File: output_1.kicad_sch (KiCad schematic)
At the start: 5 parts, among them U302 MIC2097-1YMT-TR

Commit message: Update CC resistors with feedback
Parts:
- TP? (x2): footprint 2usb:TestPoint_SM -> 2usb:TestPoint_MD
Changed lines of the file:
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@@
       (effects (font (size 1.27 1.27)) (justify right))
     )
-    (property "Footprint" "2usb:TestPoint_SM" (at 106.68 104.14 0)
+    (property "Footprint" "2usb:TestPoint_MD" (at 106.68 104.14 0)
       (effects (font (size 1.27 1.27)) hide)
     )
@@
       (effects (font (size 1.27 1.27)) (justify left))
     )
-    (property "Footprint" "2usb:TestPoint_SM" (at 116.84 101.6 0)
+    (property "Footprint" "2usb:TestPoint_MD" (at 116.84 101.6 0)
       (effects (font (size 1.27 1.27)) hide)
     )

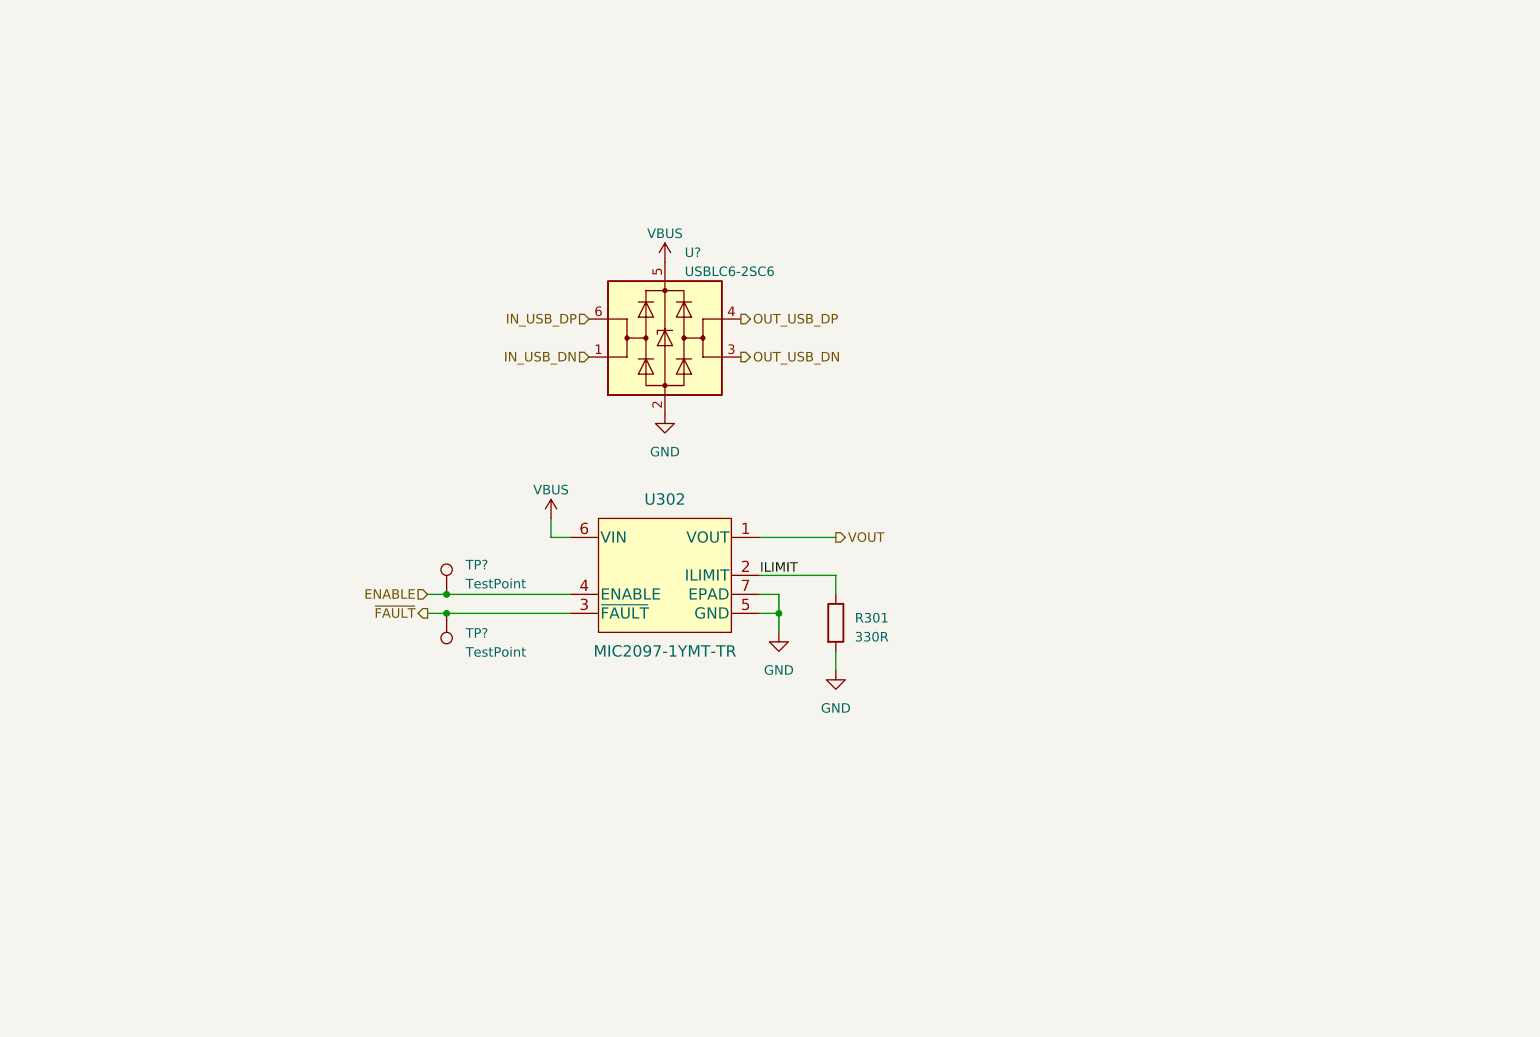
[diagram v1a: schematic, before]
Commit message: Add power switch ic and channel config ic
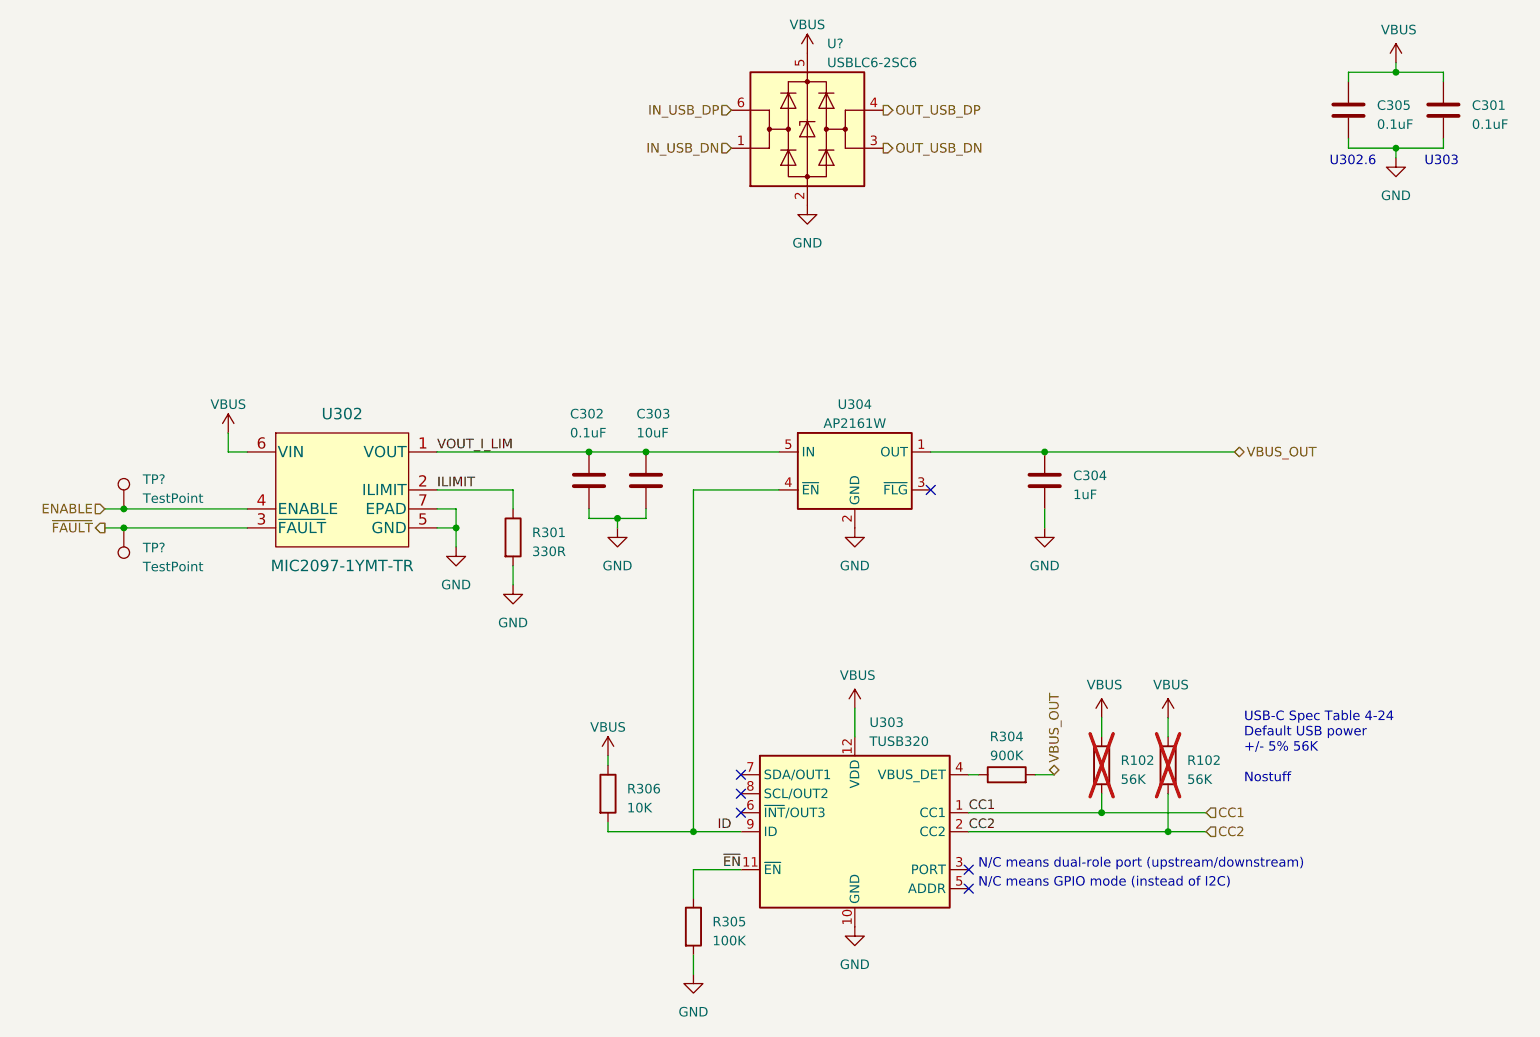
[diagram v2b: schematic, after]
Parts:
- added C301, C302, C305: 0.1uF, Capacitor_SMD:C_0201_0603Metric, symbol Device:C
- added C303: 10uF, Capacitor_SMD:C_0201_0603Metric, symbol Device:C
- added C304: 1uF, Capacitor_SMD:C_0201_0603Metric, symbol Device:C
- added R102 (x2): 56K, Resistor_SMD:R_0201_0603Metric, symbol Device:R
- added R304: 900K, Resistor_SMD:R_0201_0603Metric, symbol Device:R
- added R305: 100K, Resistor_SMD:R_0201_0603Metric, symbol Device:R
- added R306: 10K, symbol Device:R
- added U303: TUSB320, Package_DFN_QFN:Texas_X2QFN-12_1.6x1.6mm_P0.4mm, symbol Interface_USB:TUSB320
- added U304: AP2161W, symbol Power_Management:AP2161W
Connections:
- net GND: now also C301.1, C302.1, C303.1, C304.1, C305.1, R305.2, U303.10 (GND), U304.2 (GND)
- net VBUS: now also C301.2, C305.2, R102.2, R102.2, R306.1, U303.12 (VDD)
- net VOUT renamed VOUT_I_LIM
- net VOUT_I_LIM: now also C302.2, C303.2, U304.5 (IN)
- new net: R304.1, U303.4 (VBUS_DET)
- new net CC1: R102.1, U303.1 (CC1)
- new net CC2: R102.1, U303.2 (CC2)
- new net ID: R306.2, U303.9 (ID), U304.4 (~{EN})
- new net VBUS_OUT: C304.2, R304.2, U304.1 (OUT)
- new net ~{EN}: R305.1, U303.11 (~{EN})
- no-connect marks 0 -> 6
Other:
- note added: "N/C means GPIO mode (instead of I2C)"
- note added: "N/C means dual-role port (upstream/downstream)"
- note added: "U302.6"
- note added: "U303"
- note added: "USB-C Spec Table 4-24 Default USB power +/- 5% 56K Nostuff"
- moved on the sheet: R301, TP?, U302, U?

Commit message: Layout checkpoint
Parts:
- removed U304: AP2161W, symbol Power_Management:AP2161W
- added U304: AP2161W, 2usb:SON50P181X201X60-7N, symbol 2usb:AP2161W
- R306: footprint (none) -> Resistor_SMD:R_0201_0603Metric
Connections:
- net GND: now also U304.1 (GND), U304.7 (PAD)
- net ID: now also U304.3 (~{FLG})
- net VBUS_OUT: now also U304.5 (OUT), U304.6 (OUT)
- net VOUT_I_LIM: now also U304.2 (IN)
- net VBUS_DET: now reaches R304.1, U303.4 (VBUS_DET)
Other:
- moved on the sheet: R102, R304

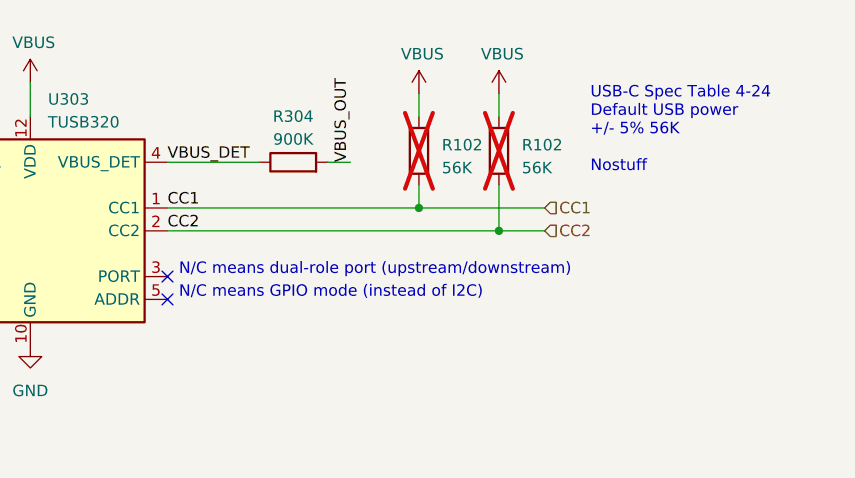
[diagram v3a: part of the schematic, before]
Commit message: Update schematic with feedback
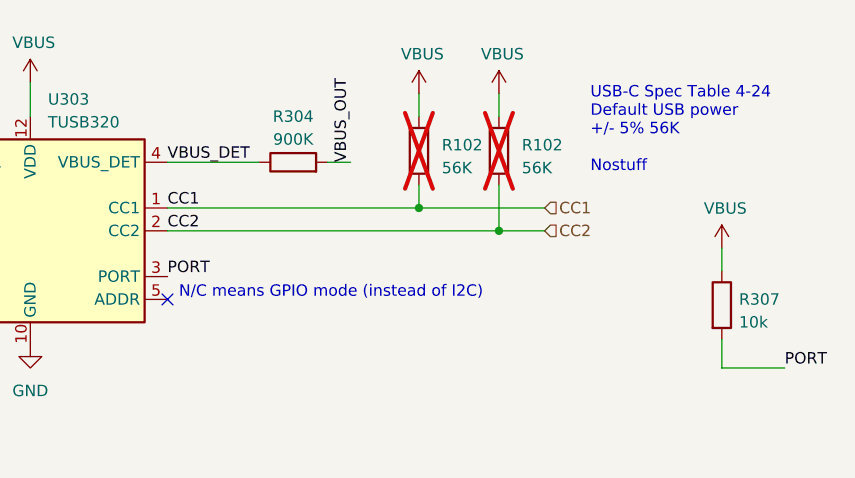
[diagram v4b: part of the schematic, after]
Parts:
- added R307: 10k, Resistor_SMD:R_0201_0603Metric, symbol Device:R
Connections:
- net VBUS: now also R307.1
- net PORT: now reaches U303.3 (PORT)
- net PORT: now also R307.2
- no-connect marks 6 -> 5
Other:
- note removed: "N/C means dual-role port (upstream/downstream)"
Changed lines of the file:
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@@
   )
   (no_connect (at 151.13 128.27))
-  (no_connect (at 181.61 138.43))
   (no_connect (at 151.13 130.81))
   (no_connect (at 151.13 125.73))
@@
     (stroke (width 0) (type default))
   )
+  (wire (pts (xy 243.205 135.255) (xy 243.205 137.795))
+    (stroke (width 0) (type default))
+  )
   (wire (pts (xy 133.35 132.08) (xy 133.35 133.35))
     (stroke (width 0) (type default))
@@
     (stroke (width 0) (type default))
   )
+  (wire (pts (xy 243.205 148.59) (xy 250.19 148.59))
+    (stroke (width 0) (type default))
+  )
   (wire (pts (xy 133.35 133.35) (xy 144.78 133.35))
     (stroke (width 0) (type default))
@@
   )
   (wire (pts (xy 134.62 91.44) (xy 134.62 92.71))
+    (stroke (width 0) (type default))
+  )
+  (wire (pts (xy 243.205 148.59) (xy 243.205 145.415))
     (stroke (width 0) (type default))
   )
@@
     (effects (font (size 1.27 1.27)) (justify left bottom))
   )
-  (text "N/C means dual-role port (upstream/downstream)" (at 182.88 138.43 0)
-    (effects (font (size 1.27 1.27)) (justify left bottom))
-  )
   (text "N/C means GPIO mode (instead of I2C)" (at 182.88 140.97 0)
     (effects (font (size 1.27 1.27)) (justify left bottom))
@@
     (effects (font (size 1.27 1.27)) (justify left bottom))
   )
+  (label "PORT" (at 181.61 138.43 0) (fields_autoplaced)
+    (effects (font (size 1.27 1.27)) (justify left bottom))
+  )
   (label "VBUS_DET" (at 181.61 125.73 0) (fields_autoplaced)
     (effects (font (size 1.27 1.27)) (justify left bottom))
@@
   )
   (label "VBUS_OUT" (at 176.53 82.55 0) (fields_autoplaced)
+    (effects (font (size 1.27 1.27)) (justify left bottom))
+  )
+  (label "PORT" (at 250.19 148.59 0) (fields_autoplaced)
     (effects (font (size 1.27 1.27)) (justify left bottom))
   )
@@
     )
   )
+  (symbol (lib_id "power:VBUS") (at 243.205 135.255 0) (unit 1)
+    (in_bom yes) (on_board yes) (dnp no)
+    (property "Reference" "#PWR0105" (at 243.205 139.065 0)
+      (effects (font (size 1.27 1.27)) hide)
+    )
+    (property "Value" "VBUS" (at 243.586 130.8608 0)
+      (effects (font (size 1.27 1.27)))
+    )
+    (property "Footprint" "" (at 243.205 135.255 0)
+      (effects (font (size 1.27 1.27)) hide)
+    )
+    (property "Datasheet" "" (at 243.205 135.255 0)
+      (effects (font (size 1.27 1.27)) hide)
+    )
+    (pin "1")
+    (instances
+      (project "2usbc"
+        (path "/dd4f7be7-d725-4a95-9fbf-108927ba51c4"
+          (reference "#PWR0105") (unit 1)
+        )
+        (path "/dd4f7be7-d725-4a95-9fbf-108927ba51c4/4d5e1fa8-a369-4929-bc9f-9e0c30bbf1a7"
+          (reference "#PWR0334") (unit 1)
+        )
+        (path "/dd4f7be7-d725-4a95-9fbf-108927ba51c4/a714a7b2-eec6-4585-9cc0-17dfa16154ee"
+          (reference "#PWR0417") (unit 1)
+        )
+      )
+    )
+  )
   (symbol (lib_id "Connector:TestPoint") (at 68.58 90.17 0) (unit 1)
     (in_bom yes) (on_board yes) (dnp no) (fields_autoplaced)
@@
         )
       )
+    )
+  )
+  (symbol (lib_id "Device:R") (at 243.205 141.605 0) (unit 1)
+    (in_bom yes) (on_board yes) (dnp no) (fields_autoplaced)
+    (property "Reference" "R307" (at 245.11 140.97 0)
+      (effects (font (size 1.27 1.27)) (justify left))
+    )
+    (property "Value" "10k" (at 245.11 143.51 0)
+      (effects (font (size 1.27 1.27)) (justify left))
+    )
+    (property "Footprint" "Resistor_SMD:R_0201_0603Metric" (at 241.427 141.605 90)
+      (effects (font (size 1.27 1.27)) hide)
+    )
+    (property "Datasheet" "~" (at 243.205 141.605 0)
+      (effects (font (size 1.27 1.27)) hide)
+    )
+    (pin "1")
+    (pin "2")
+    (instances
+      (project "2usbc"
+        (path "/dd4f7be7-d725-4a95-9fbf-108927ba51c4/4d5e1fa8-a369-4929-bc9f-9e0c30bbf1a7"
+          (reference "R307") (unit 1)
+        )
+        (path "/dd4f7be7-d725-4a95-9fbf-108927ba51c4/a714a7b2-eec6-4585-9cc0-17dfa16154ee"
+          (reference "R407") (unit 1)
+        )
+      )
